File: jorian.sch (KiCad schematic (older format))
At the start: 103 parts, among them J1 MicroUSB, J2 USB-C, J3 MicroUSB, J4 USB-C, J5 MJ-4PP-9, SW1 SW_SPDT, U3 AMS1117, U4 TP4056, U5 DW01A, U6 FS8205A

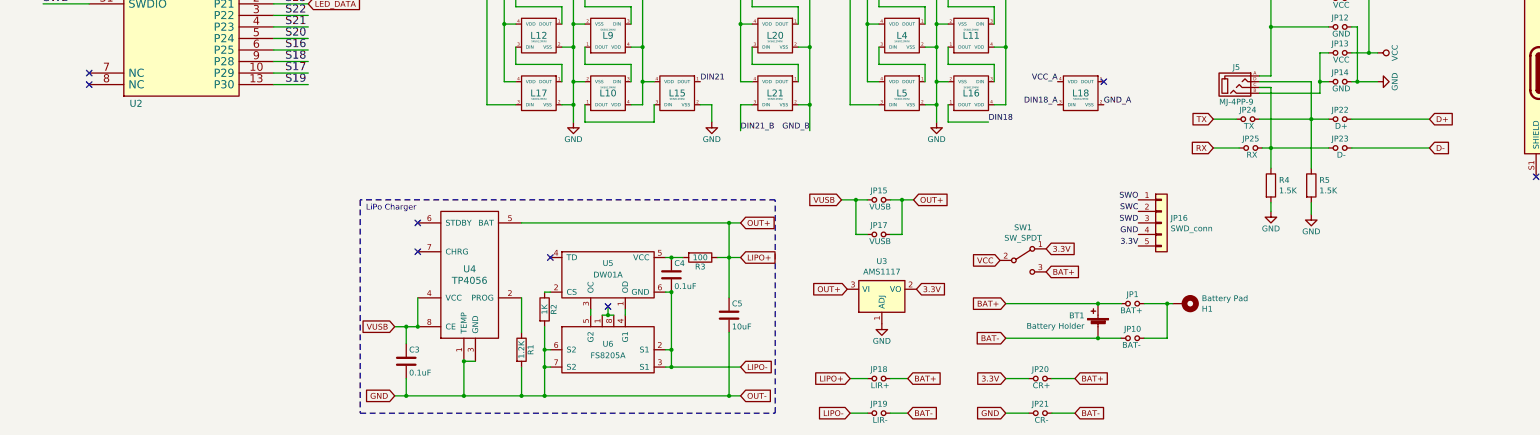
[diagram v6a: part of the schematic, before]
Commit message: autorouted alpha, better placement
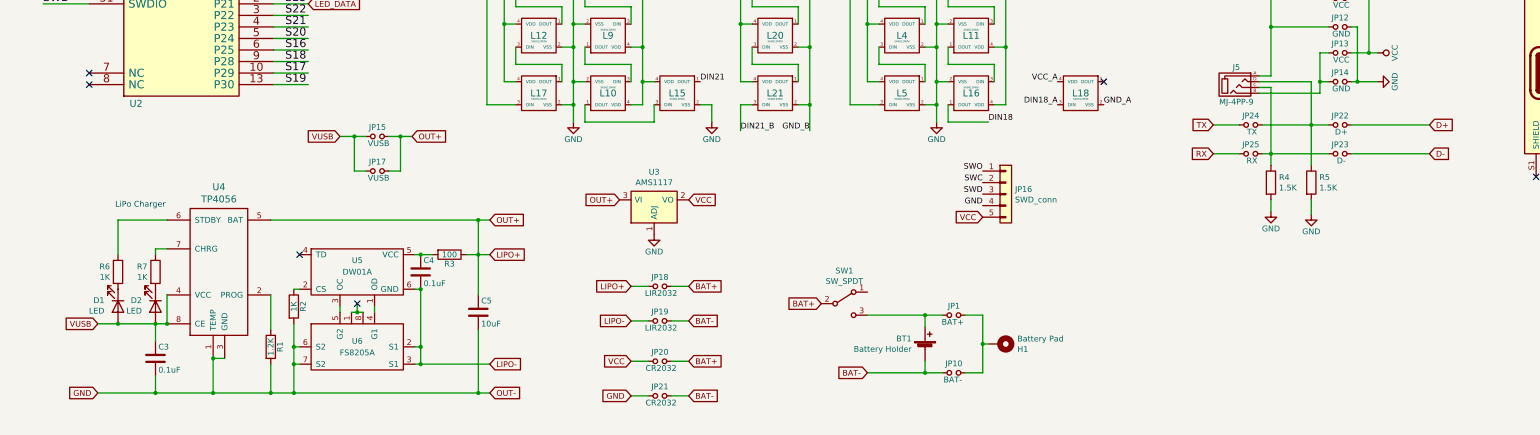
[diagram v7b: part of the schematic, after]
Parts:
- added D1, D2: LED, kbd:R_0805, symbol Device:LED
- added R6, R7: 1K, kbd:R_0805, symbol Device:R
- JP18: value LIR+ -> LIR2032
- JP19: value LIR- -> LIR2032
- JP20: value CR+ -> CR2032
- JP21: value CR- -> CR2032
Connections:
- net labels removed: 3.3V
- wire segments 403 -> 411
- no-connect marks 25 -> 23
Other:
- moved on the sheet: BT1, C3, C4, C5, H1, JP1, JP10, JP15, JP16, JP17, JP18, JP19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

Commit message: updated placement
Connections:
- wire segments 411 -> 417
- no-connect marks 23 -> 24
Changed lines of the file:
@@
 $EndComp
 Wire Wire Line
-	14700 7100 14700 7200
-Wire Wire Line
-	14700 7300 14700 7400
-Text Label 14700 7150 0    50   ~ 0
-D-
-Text Label 14700 7350 0    50   ~ 0
-D+
-Text Label 14900 5250 0    50   ~ 0
-D+
-Text Label 14900 5350 0    50   ~ 0
-D-
+	14700 7100 14700 7150
+Wire Wire Line
+	14700 7300 14700 7350
 NoConn ~ 14700 7800
 NoConn ~ 14700 7700
@@
 NoConn ~ 16150 6900
 NoConn ~ 16150 6800
-Text Label 15650 5350 0    50   ~ 0
-D-
-Text Label 15650 5250 0    50   ~ 0
-D+
-Text Label 16150 7300 0    50   ~ 0
-D+
-Text Label 16150 7100 0    50   ~ 0
-D-
 Text Label 15650 5050 0    50   ~ 0
 VUSB
@@
 Wire Wire Line
 	3950 7750 4050 7750
-Text GLabel 12875 7650 2    50   Input ~ 0
+Text GLabel 12425 7650 2    50   Input ~ 0
 D+
-Text GLabel 12875 7900 2    50   Input ~ 0
+Text GLabel 12425 7900 2    50   Input ~ 0
 D-
 $Comp
@@
 F 3 "" H 11500 8400 50  0001 C CNN
 	1    11500 8400
-	-1   0    0    -1
+	1    0    0    -1
 $EndComp
 Wire Wire Line
 	11500 8300 11500 8400
 Wire Wire Line
-	12200 7900 12875 7900
+	12200 7900 12425 7900
 $Comp
 L Device:Jumper_NO_Small JP24
@@
 L power:GND #PWR0126
 U 1 1 5F65E379
-P 11850 8425
-F 0 "#PWR0126" H 11850 8175 50  0001 C CNN
-F 1 "GND" H 11850 8275 50  0000 C CNN
-F 2 "" H 11850 8425 50  0001 C CNN
-F 3 "" H 11850 8425 50  0001 C CNN
-	1    11850 8425
+P 11850 8400
+F 0 "#PWR0126" H 11850 8150 50  0001 C CNN
+F 1 "GND" H 11850 8250 50  0000 C CNN
+F 2 "" H 11850 8400 50  0001 C CNN
+F 3 "" H 11850 8400 50  0001 C CNN
+	1    11850 8400
 	-1   0    0    -1
 $EndComp
 Wire Wire Line
-	11850 8300 11850 8425
-Wire Wire Line
-	12200 7650 12875 7650
+	12200 7650 12425 7650
 Wire Wire Line
 	11925 7375 11925 7275
@@
 Text GLabel 7600 9200 0    50   Input ~ 0
 BAT+
+NoConn ~ 8000 9100
+Text GLabel 14800 7150 2    50   Input ~ 0
+D-
+Text GLabel 14800 7350 2    50   Input ~ 0
+D+
+Wire Wire Line
+	14700 7150 14800 7150
+Connection ~ 14700 7150
+Wire Wire Line
+	14700 7150 14700 7200
+Wire Wire Line
+	14700 7350 14800 7350
+Connection ~ 14700 7350
+Wire Wire Line
+	14700 7350 14700 7400
+Text GLabel 16250 7150 2    50   Input ~ 0
+D-
+Text GLabel 16250 7350 2    50   Input ~ 0
+D+
+Wire Wire Line
+	16150 7150 16250 7150
+Wire Wire Line
+	16150 7350 16250 7350
+Text GLabel 14900 5250 2    50   Input ~ 0
+D+
+Text GLabel 14900 5350 2    50   Input ~ 0
+D-
+Text GLabel 15650 5350 2    50   Input ~ 0
+D-
+Text GLabel 15650 5250 2    50   Input ~ 0
+D+
+Wire Wire Line
+	11850 8300 11850 8400
 $EndSCHEMATC
